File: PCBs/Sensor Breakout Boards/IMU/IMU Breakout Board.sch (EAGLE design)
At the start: 5 parts, among them J1 2X6 FEMALE, U1 ICM_20649

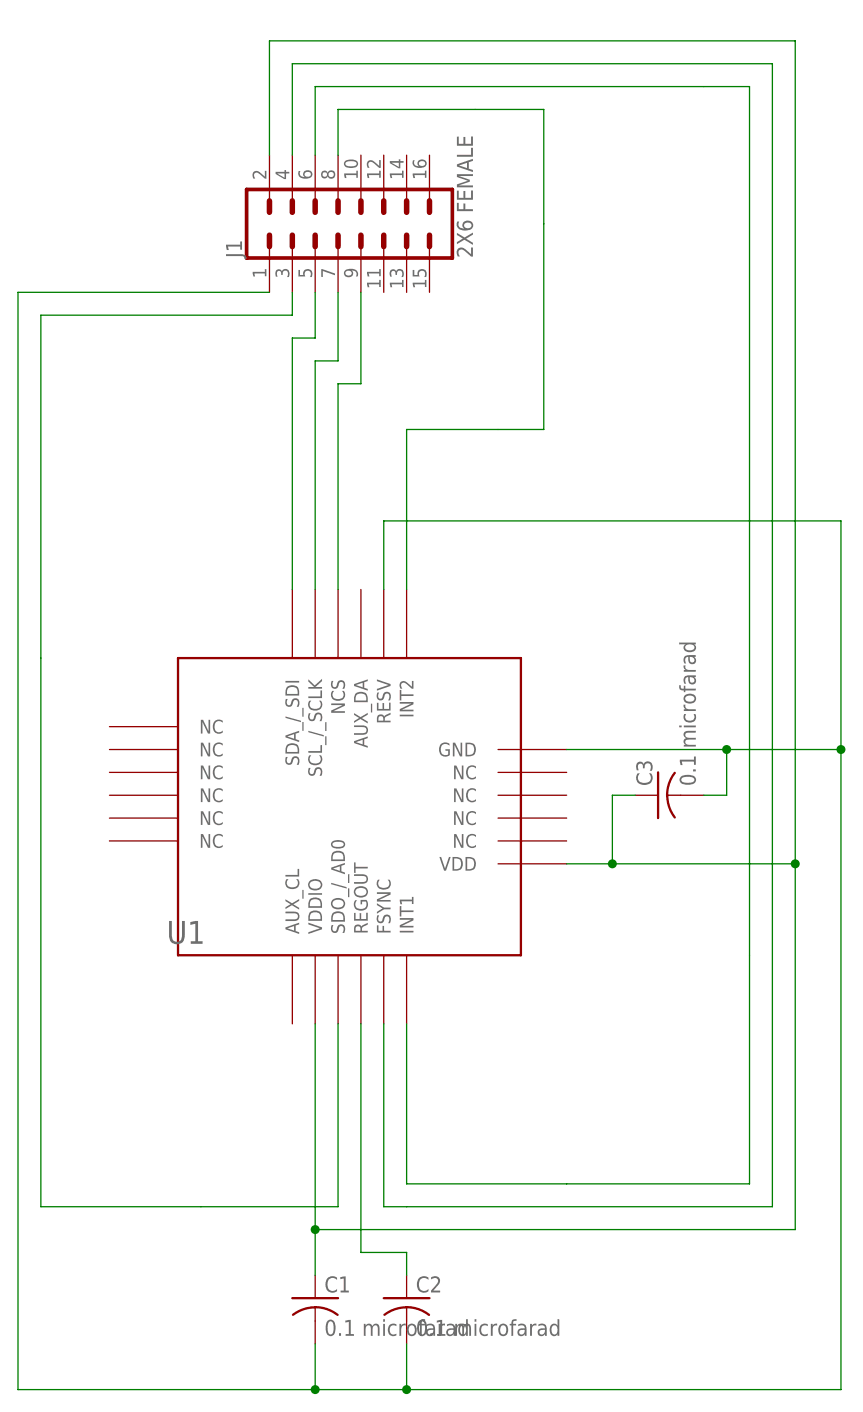
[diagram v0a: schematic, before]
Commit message: rev 2 imu board complete
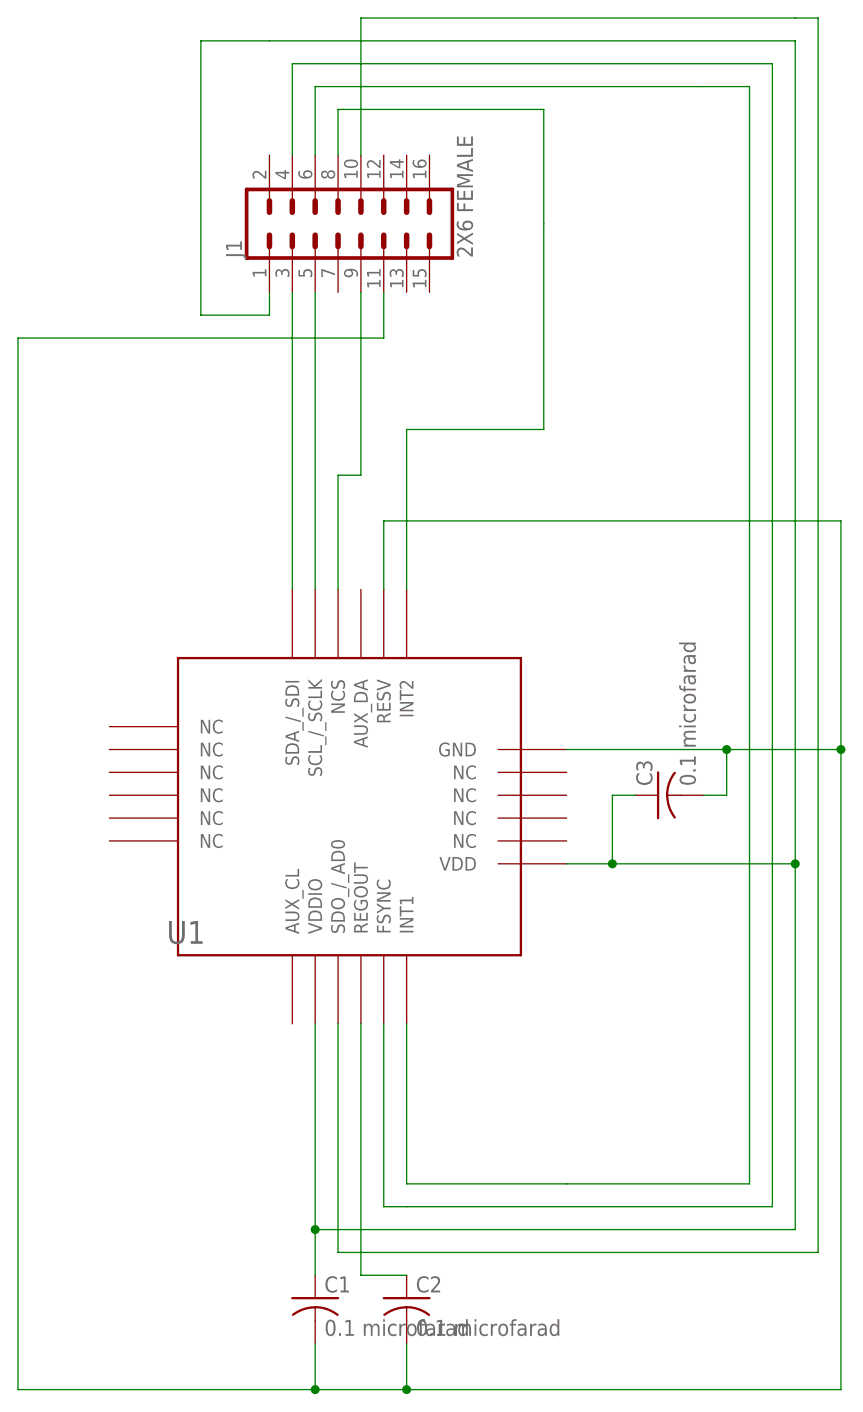
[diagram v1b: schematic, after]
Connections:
- net N$11: now also J1.11; no longer J1.1
- net N$5: now also J1.3, U1.SDA_/_SDI; no longer J1.7, U1.SCL_/_SCLK
- net N$6: now also U1.SCL_/_SCLK; no longer U1.SDA_/_SDI
- net N$7: now also J1.10; no longer J1.3
- net N$8: now also J1.1; no longer J1.2
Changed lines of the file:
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@@
 <net name="N$4" class="0">
 <segment>
-<wire x1="17.78" y1="40.64" x2="17.78" y2="63.5" width="0.1524" layer="91"/>
-<wire x1="17.78" y1="63.5" x2="20.32" y2="63.5" width="0.1524" layer="91"/>
+<wire x1="17.78" y1="40.64" x2="17.78" y2="53.34" width="0.1524" layer="91"/>
+<wire x1="17.78" y1="53.34" x2="20.32" y2="53.34" width="0.1524" layer="91"/>
 <pinref part="J1" gate="G$1" pin="9"/>
-<wire x1="20.32" y1="63.5" x2="20.32" y2="73.66" width="0.1524" layer="91"/>
+<wire x1="20.32" y1="53.34" x2="20.32" y2="73.66" width="0.1524" layer="91"/>
 <pinref part="U1" gate="G1" pin="NCS"/>
-</segment>
-</net>
-<net name="N$5" class="0">
-<segment>
-<wire x1="15.24" y1="40.64" x2="15.24" y2="66.04" width="0.1524" layer="91"/>
-<wire x1="15.24" y1="66.04" x2="17.78" y2="66.04" width="0.1524" layer="91"/>
-<pinref part="J1" gate="G$1" pin="7"/>
-<wire x1="17.78" y1="66.04" x2="17.78" y2="73.66" width="0.1524" layer="91"/>
-<pinref part="U1" gate="G1" pin="SCL_/_SCLK"/>
-</segment>
-</net>
-<net name="N$6" class="0">
-<segment>
-<wire x1="12.7" y1="40.64" x2="12.7" y2="68.58" width="0.1524" layer="91"/>
-<wire x1="12.7" y1="68.58" x2="15.24" y2="68.58" width="0.1524" layer="91"/>
-<pinref part="J1" gate="G$1" pin="5"/>
-<wire x1="15.24" y1="68.58" x2="15.24" y2="73.66" width="0.1524" layer="91"/>
-<pinref part="U1" gate="G1" pin="SDA_/_SDI"/>
-</segment>
-</net>
-<net name="N$7" class="0">
-<segment>
-<wire x1="17.78" y1="-7.62" x2="17.78" y2="-27.94" width="0.1524" layer="91"/>
-<wire x1="17.78" y1="-27.94" x2="2.54" y2="-27.94" width="0.1524" layer="91"/>
-<wire x1="2.54" y1="-27.94" x2="-15.24" y2="-27.94" width="0.1524" layer="91"/>
-<wire x1="-15.24" y1="-27.94" x2="-15.24" y2="33.02" width="0.1524" layer="91"/>
-<wire x1="-15.24" y1="33.02" x2="-15.24" y2="71.12" width="0.1524" layer="91"/>
-<wire x1="-15.24" y1="71.12" x2="12.7" y2="71.12" width="0.1524" layer="91"/>
-<pinref part="J1" gate="G$1" pin="3"/>
-<wire x1="12.7" y1="71.12" x2="12.7" y2="73.66" width="0.1524" layer="91"/>
-<pinref part="U1" gate="G1" pin="SDO_/_AD0"/>
 </segment>
 </net>
 <net name="N$8" class="0">
 <segment>
-<pinref part="J1" gate="G$1" pin="2"/>
-<wire x1="10.16" y1="88.9" x2="10.16" y2="101.6" width="0.1524" layer="91"/>
 <wire x1="10.16" y1="101.6" x2="68.58" y2="101.6" width="0.1524" layer="91"/>
 <wire x1="68.58" y1="101.6" x2="68.58" y2="10.16" width="0.1524" layer="91"/>
@@
 <junction x="68.58" y="10.16"/>
 <junction x="48.26" y="10.16"/>
+<wire x1="10.16" y1="101.6" x2="2.54" y2="101.6" width="0.1524" layer="91"/>
+<wire x1="2.54" y1="101.6" x2="2.54" y2="71.12" width="0.1524" layer="91"/>
+<wire x1="2.54" y1="71.12" x2="10.16" y2="71.12" width="0.1524" layer="91"/>
+<pinref part="J1" gate="G$1" pin="1"/>
+<wire x1="10.16" y1="71.12" x2="10.16" y2="73.66" width="0.1524" layer="91"/>
 </segment>
 </net>
 <net name="N$9" class="0">
 <segment>
-<wire x1="20.32" y1="-7.62" x2="20.32" y2="-33.02" width="0.1524" layer="91"/>
-<wire x1="20.32" y1="-33.02" x2="25.4" y2="-33.02" width="0.1524" layer="91"/>
-<wire x1="25.4" y1="-33.02" x2="25.4" y2="-35.56" width="0.1524" layer="91"/>
+<wire x1="20.32" y1="-7.62" x2="20.32" y2="-35.56" width="0.1524" layer="91"/>
+<wire x1="20.32" y1="-35.56" x2="25.4" y2="-35.56" width="0.1524" layer="91"/>
 <pinref part="U1" gate="G1" pin="REGOUT"/>
 <pinref part="C2" gate="G$1" pin="1"/>
@@
 <segment>
 <wire x1="25.4" y1="-43.18" x2="25.4" y2="-48.26" width="0.1524" layer="91"/>
-<pinref part="J1" gate="G$1" pin="1"/>
-<wire x1="10.16" y1="73.66" x2="-17.78" y2="73.66" width="0.1524" layer="91"/>
-<wire x1="-17.78" y1="73.66" x2="-17.78" y2="-48.26" width="0.1524" layer="91"/>
+<wire x1="-17.78" y1="68.58" x2="-17.78" y2="-48.26" width="0.1524" layer="91"/>
 <wire x1="-17.78" y1="-48.26" x2="15.24" y2="-48.26" width="0.1524" layer="91"/>
 <wire x1="15.24" y1="-48.26" x2="25.4" y2="-48.26" width="0.1524" layer="91"/>
@@
 <junction x="60.96" y="22.86"/>
 <junction x="73.66" y="22.86"/>
+<pinref part="J1" gate="G$1" pin="11"/>
+<wire x1="22.86" y1="73.66" x2="22.86" y2="68.58" width="0.1524" layer="91"/>
+<wire x1="22.86" y1="68.58" x2="-17.78" y2="68.58" width="0.1524" layer="91"/>
 </segment>
 </net>
+<net name="N$5" class="0">
+<segment>
+<pinref part="J1" gate="G$1" pin="3"/>
+<pinref part="U1" gate="G1" pin="SDA_/_SDI"/>
+<wire x1="12.7" y1="73.66" x2="12.7" y2="40.64" width="0.1524" layer="91"/>
+</segment>
+</net>
+<net name="N$6" class="0">
+<segment>
+<pinref part="U1" gate="G1" pin="SCL_/_SCLK"/>
+<pinref part="J1" gate="G$1" pin="5"/>
+<wire x1="15.24" y1="40.64" x2="15.24" y2="73.66" width="0.1524" layer="91"/>
+</segment>
+</net>
+<net name="N$7" class="0">
+<segment>
+<pinref part="U1" gate="G1" pin="SDO_/_AD0"/>
+<wire x1="17.78" y1="-7.62" x2="17.78" y2="-33.02" width="0.1524" layer="91"/>
+<wire x1="17.78" y1="-33.02" x2="71.12" y2="-33.02" width="0.1524" layer="91"/>
+<wire x1="71.12" y1="-33.02" x2="71.12" y2="104.14" width="0.1524" layer="91"/>
+<wire x1="71.12" y1="104.14" x2="68.58" y2="104.14" width="0.1524" layer="91"/>
+<pinref part="J1" gate="G$1" pin="10"/>
+<wire x1="68.58" y1="104.14" x2="20.32" y2="104.14" width="0.1524" layer="91"/>
+<wire x1="20.32" y1="104.14" x2="20.32" y2="88.9" width="0.1524" layer="91"/>
+</segment>
+</net>

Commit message: Added ground planes
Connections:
- net N$11 renamed GND
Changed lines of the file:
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@@
 </segment>
 </net>
-<net name="N$11" class="0">
+<net name="GND" class="0">
 <segment>
 <wire x1="25.4" y1="-43.18" x2="25.4" y2="-48.26" width="0.1524" layer="91"/>
